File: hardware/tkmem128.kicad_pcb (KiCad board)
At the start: 2 copper layers, 78.7 x 66 mm, 24 parts, among them J1 Barramento TK, U1 GAL20V8B, U2 74HCT273, U3 AS6C1008-55PCN, U4 27C256

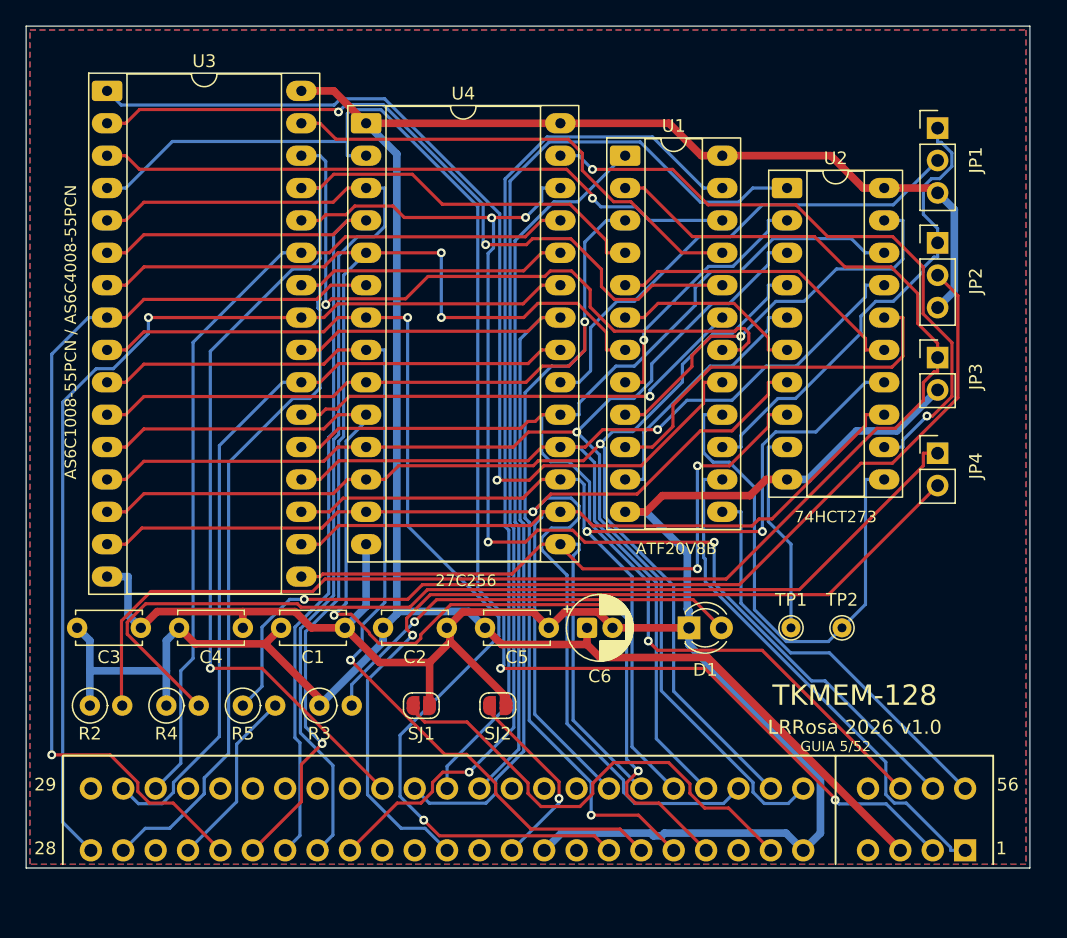
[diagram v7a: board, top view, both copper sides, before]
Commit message: Rasgo da guia 2 mm mais fundo e serigrafia em negrito
Conferencia em papel do Leonardo (impressao 1:1 contra as pecas reais, jul/2026):
todas as medidas e alinhamentos bateram. Uma correcao saiu dela.

RASGO DA GUIA (tira, entre os dedos de J2): 5,0 -> 7,0 mm de profundidade. Os
5 mm nao chegavam ao fundo da guia do conector. Agora vai de y=45,00 a y=38,00.

  folga lateral ate o cobre mais proximo (pinos 4/6/51/53)   0,88 mm
  quanto ainda daria para aprofundar                         0,62 mm

Esses 0,62 mm sao o limite: os dedos comecam em y=37,38. Passar disso obriga a
encurta-los tambem. Anotado no item 3 de ANTES-DE-FABRICAR.

A profundidade virou parametro (KEYSLOT_DEPTH em netlist_exp.py) em vez de
numero solto no gen_pcb.py, e ganhou tools/ajusta_guia.py para aplicar numa
placa ja roteada — refaz o contorno e repreenche as zonas.

O primeiro recorte deixou orfao o fundo do rasgo antigo: um traco de Edge.Cuts
solto no meio da placa, que nenhum DRC acusa e o fabricante cortaria. Filtrar
tracos por posicao e fragil, entao ajusta_guia.py reconstroi o contorno inteiro
e verifica que ele fecha (cada vertice usado por exatamente dois tracos).

NEGRITO: o Leonardo pos a serigrafia da principal em negrito, para ler melhor.
Faltavam 9 referencias (C1..C6, D1, TP1, TP2) e a tira inteira. Uniformizado
nas duas placas com tools/silk_negrito.py, que segue a regra do proprio KiCad —
espessura = 0,2 x o tamanho da fonte, e nao um valor fixo, que e o que mantem
texto grande e pequeno com o mesmo peso.

Tambem: *.lck no .gitignore e os dois que tinham entrado no repositorio
removidos do indice.

DRC: principal 2 violacoes (as starved_thermal de sempre), tira 0. Alinhamento
entre as placas inalterado.

Co-Authored-By: Claude Opus 5 <noreply@anthropic.com>
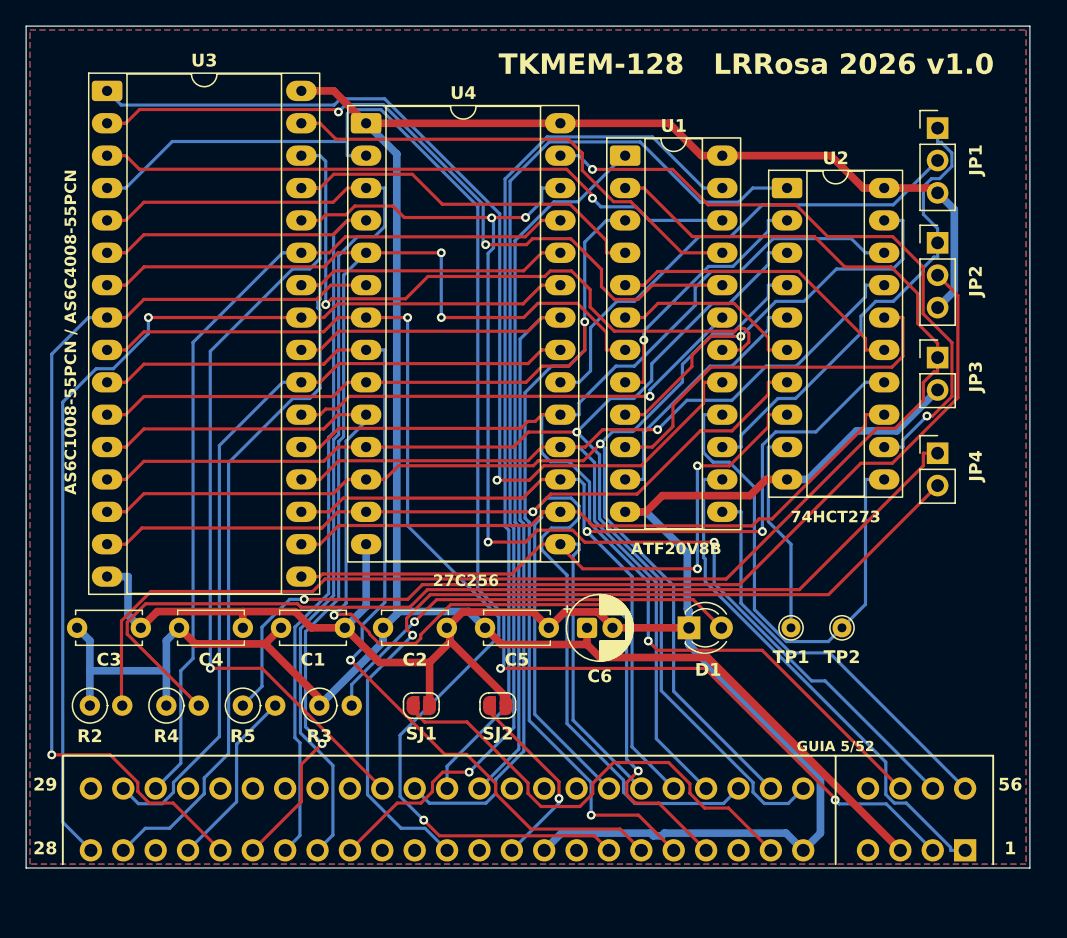
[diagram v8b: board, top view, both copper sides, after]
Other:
- board text added: "NUNCA feche JP4 em ZX Spectrum"
- board text added: "TKMEM-128 LRRosa 2026 v1.0"
- board text removed: "LRRosa 2026 v1.0"
- board text removed: "NÃO feche JP4 em ZX Spectrum: o pino 17 lá é o V do vídeo"
- board text removed: "TKMEM-128"
